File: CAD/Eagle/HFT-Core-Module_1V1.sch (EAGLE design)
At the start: 399 parts, among them Q0521 ABS07-32.768KHZ, Q0811 ABM03B-32.000MHZ, Q0911 ABM3B-16MHZ-10-R50-1-U, T1201 MMBT2222, T1202 MMBT2222, T1203 MMBT2222, U0111 STM32L4Z_144PIN_SMPS, U0431 PAM2305AAB120, U0601 LM4120IM5-3.0, U0611 MAX5217, U0631 CFPT-141-20MHZ, U0641 OPA354, U0701 Si5338, U0801 SX1276, U0901 AX5243, U0911 PE4259, U0921 PE4259, U0991 PE4259, U1101 MCP3911A0-E-SS, U1111 MAX5136AGTG+, U1121 OPA354, U1131 OPA354, U1141 OPA354, U1201 NHD-C0220BIZ_2X20CHARS, U1301 MPU-9250, U1311 MS5607-02BA03, U1321 SHT31-DIS, U1402 SPV1040T, U1501 TS5A23166, U1601 SC189ZSKTRT, U1701 TS5A23166, U1801 TS5A23166, U1901 TS5A23166, X1261 TTE_EN11-HSM, X1401 WIRE-TO-BOARD_5MM08_1X02, X2001 MOLEX 105017-0001, X2101 SMA_SMT_AMPHENOL-901-143, SAM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, X2111 SMA_SMT_AMPHENOL-901-143, SAM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, X2201 CUI SJ1-3535NS, X2211 CUI SJ1-3535NS, X2311 2X20/90_1MM27_HARWIN_M50-3202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, X2312 2X20/90_1MM27_HARWIN_M50-3202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, X2321 2X20/90_1MM27_HARWIN_M50-3202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, X2322 2X20/90_1MM27_HARWIN_M50-3202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, X2331 2X20/90_1MM27_HARWIN_M50-3202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, X2332 2X20/90_1MM27_HARWIN_M50-3202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

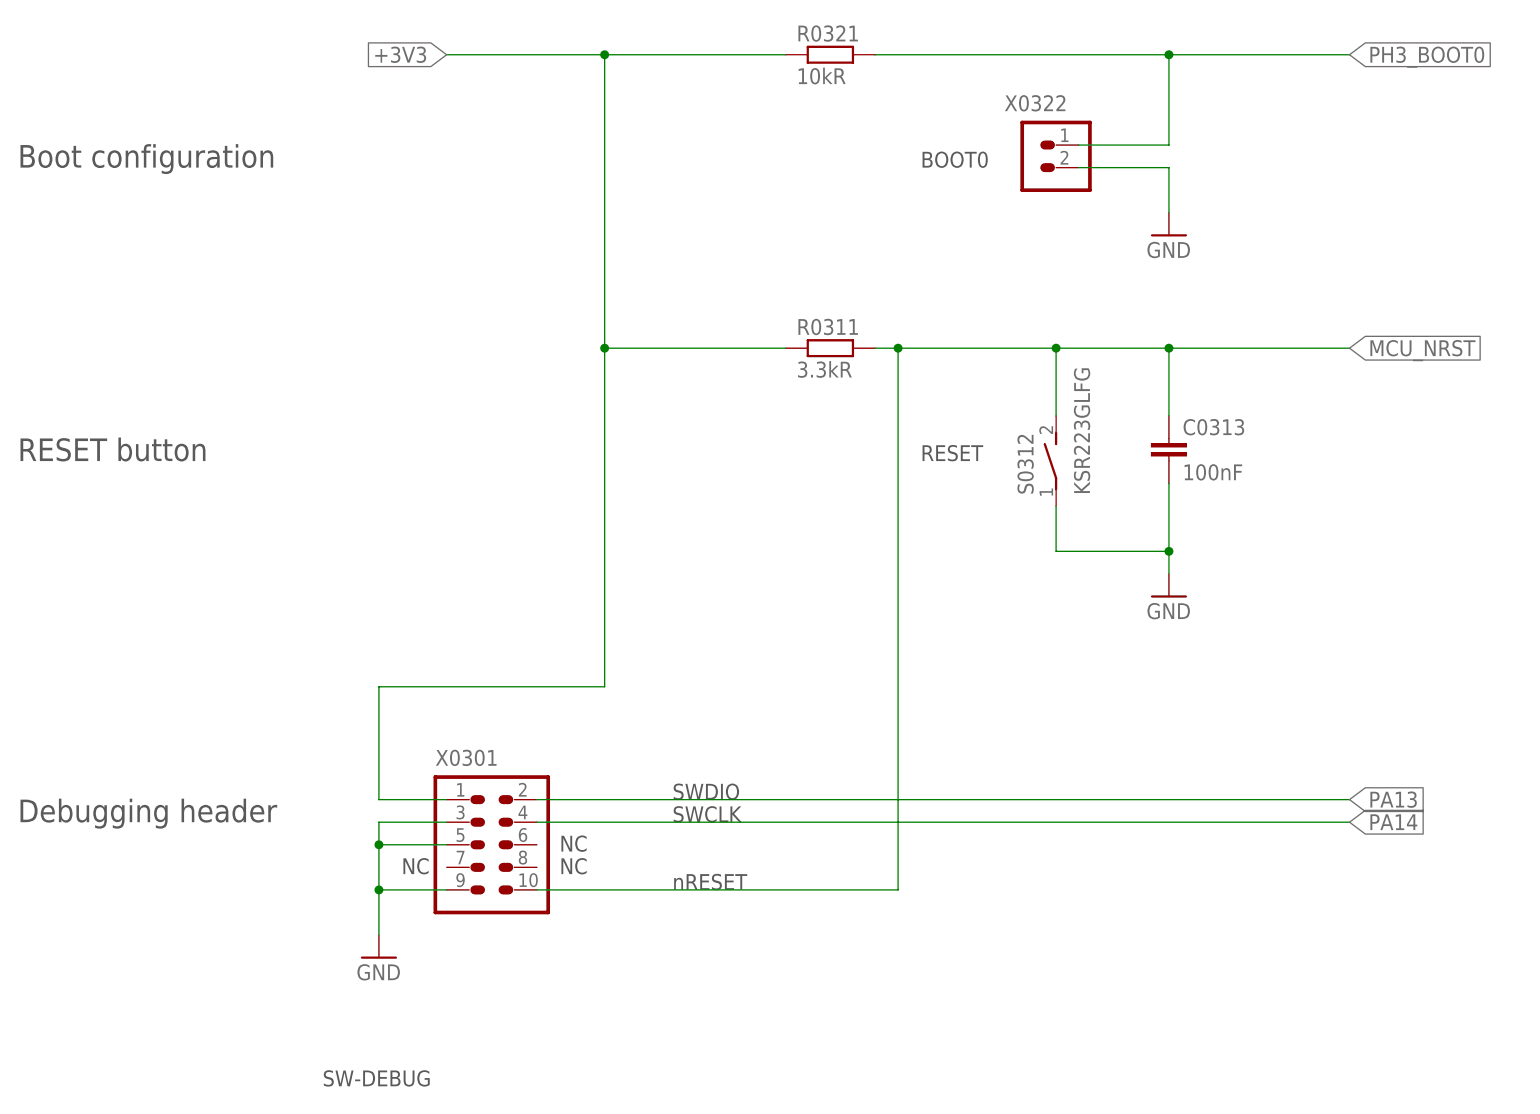
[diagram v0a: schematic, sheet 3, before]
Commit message: HW_1V1 - SWD header, XO 32.768kHz caps, RESET resistor removed, SWD resistors added
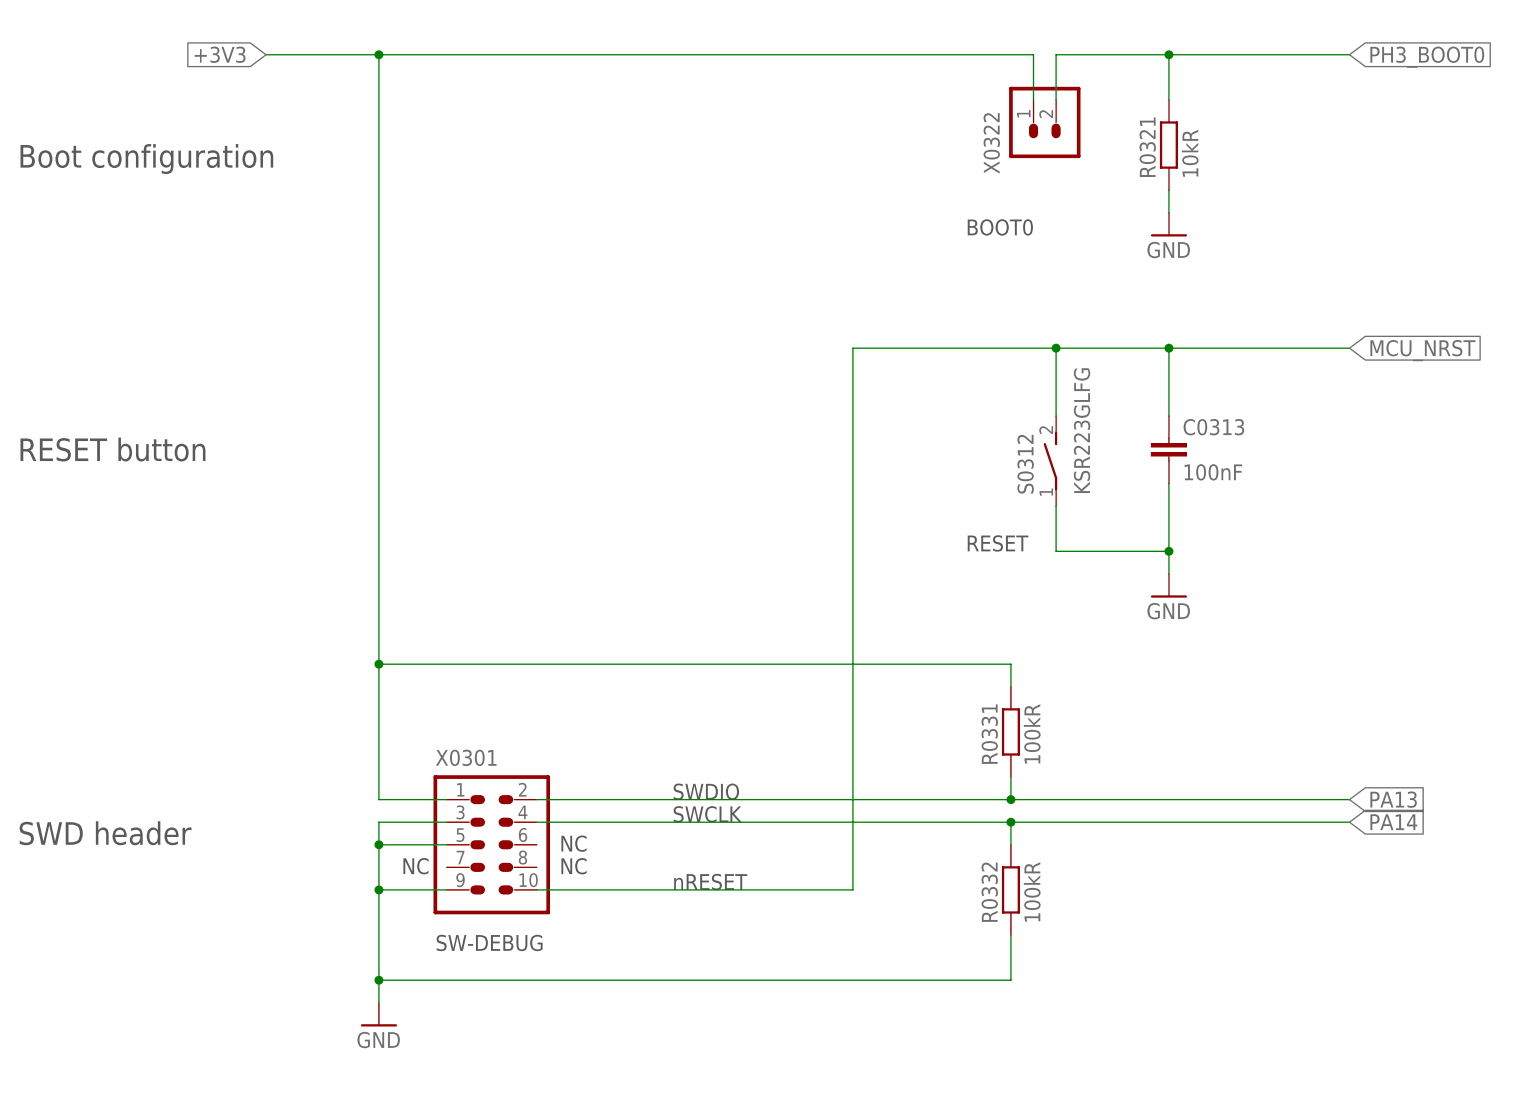
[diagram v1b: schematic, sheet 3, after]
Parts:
- removed R0311: 3.3kR, rcl:R-EU_R0603
- added C0532: 12pF, rcl:C-EUC0603
- added R0331, R0332: 100kR, rcl:R-EU_R0603
- C0511: value 1.5pF -> 18pF
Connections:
- net +3V3: now also R0331.2, X0322.1; no longer R0311.1, R0321.1
- net GND: now also C0532.2, R0321.1, R0332.1; no longer X0322.2
- net MCU_NRST: no longer R0311.2
- net PA13: now also R0331.1
- net PA14: now also R0332.2
- net PC14_MCU_OSC32_IN: now also C0532.1
- net PH3_BOOT0: now also X0322.2; no longer X0322.1
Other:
- note added: "SWD header"
- note removed: "Debugging header"
- moved on the sheet: R0321, X0322

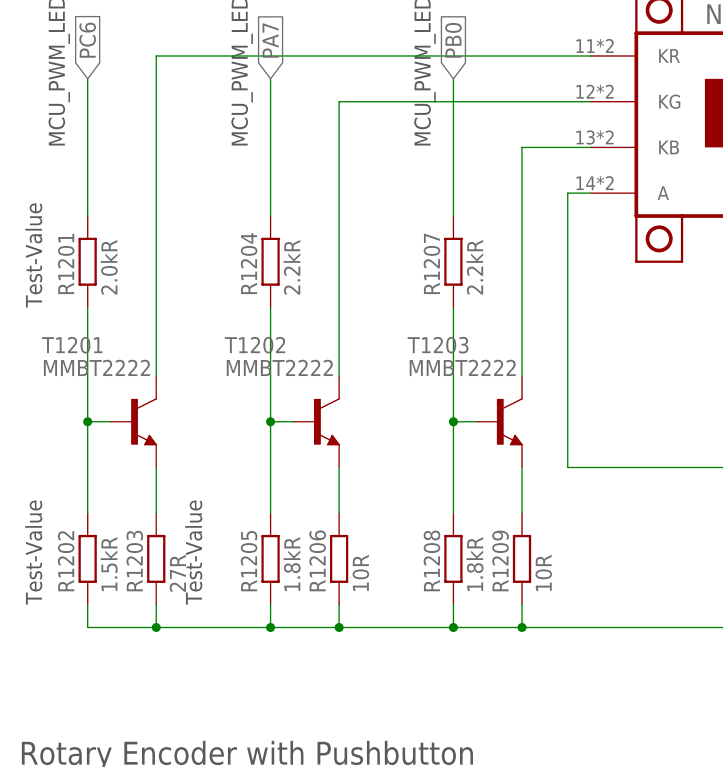
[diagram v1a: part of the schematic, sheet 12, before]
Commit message: HW_1V1 - LCD-backlight resistors changed
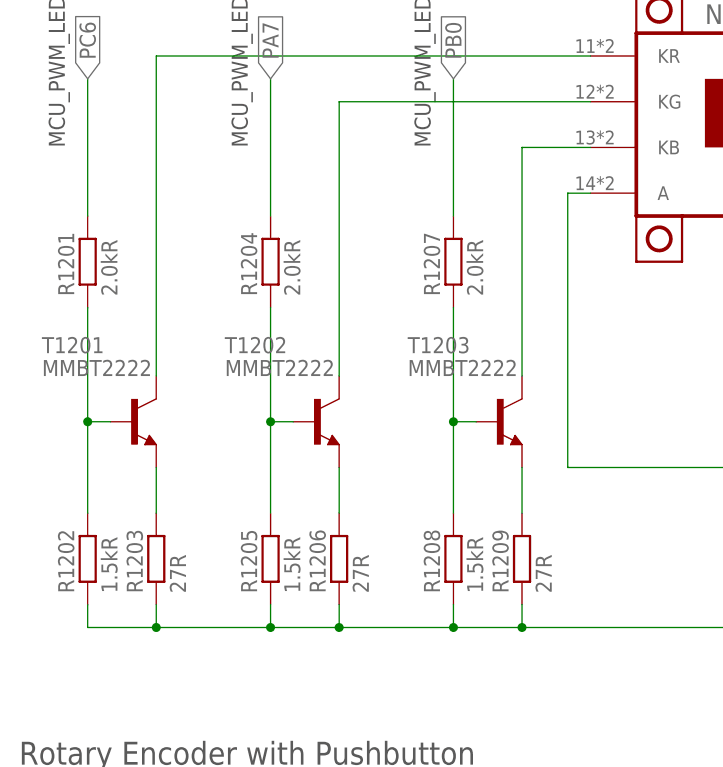
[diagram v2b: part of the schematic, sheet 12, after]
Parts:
- R1204, R1207: value 2.2kR -> 2.0kR
- R1205, R1208: value 1.8kR -> 1.5kR
- R1206, R1209: value 10R -> 27R
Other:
- note removed: "Test-Value"
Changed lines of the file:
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@@
 <part name="T1202" library="transistor" deviceset="BC846" device="" value="MMBT2222"/>
 <part name="T1203" library="transistor" deviceset="BC846" device="" value="MMBT2222"/>
-<part name="R1209" library="rcl" deviceset="R-EU_" device="R0805" value="10R"/>
-<part name="R1208" library="rcl" deviceset="R-EU_" device="R0603" value="1.8kR"/>
-<part name="R1207" library="rcl" deviceset="R-EU_" device="R0603" value="2.2kR"/>
-<part name="R1206" library="rcl" deviceset="R-EU_" device="R0805" value="10R"/>
+<part name="R1209" library="rcl" deviceset="R-EU_" device="R0805" value="27R"/>
+<part name="R1208" library="rcl" deviceset="R-EU_" device="R0603" value="1.5kR"/>
+<part name="R1207" library="rcl" deviceset="R-EU_" device="R0603" value="2.0kR"/>
+<part name="R1206" library="rcl" deviceset="R-EU_" device="R0805" value="27R"/>
 <part name="R1203" library="rcl" deviceset="R-EU_" device="R0805" value="27R"/>
-<part name="R1205" library="rcl" deviceset="R-EU_" device="R0603" value="1.8kR"/>
+<part name="R1205" library="rcl" deviceset="R-EU_" device="R0603" value="1.5kR"/>
 <part name="R1202" library="rcl" deviceset="R-EU_" device="R0603" value="1.5kR"/>
-<part name="R1204" library="rcl" deviceset="R-EU_" device="R0603" value="2.2kR"/>
+<part name="R1204" library="rcl" deviceset="R-EU_" device="R0603" value="2.0kR"/>
 <part name="R1201" library="rcl" deviceset="R-EU_" device="R0603" value="2.0kR"/>
 <part name="FRAME_13" library="df4iah_frame" deviceset="A4L-LOC" device="" value="Holes"/>
@@
 <text x="195.58" y="53.34" size="1.778" layer="97">MCU_IN_RE_Q</text>
 <text x="195.58" y="35.56" size="1.778" layer="97">MCU_IN_RE_PB</text>
-<text x="12.7" y="88.9" size="1.778" layer="97" rot="R90">Test-Value</text>
-<text x="12.7" y="121.92" size="1.778" layer="97" rot="R90">Test-Value</text>
-<text x="30.48" y="88.9" size="1.778" layer="97" rot="R90">Test-Value</text>
 </plain>
 <instances>

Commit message: HW_1V1 - I2C addresses changed, LCD will be replaced by EA DOGS104N-A
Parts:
- R1331, R1332: value 3.9kR -> 1.0kR
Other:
- note added: "9-axis sensor: MPU-9250 I2C addr: 0x68 / 0x0C"
- note added: "Baro sensor: MS5607-02BA03 I2C addr: 0x76"
- note added: "Clock distributor I2C addr: 0x70"
- note added: "LC-Display I2C addr: 0x3D"
- note added: "LCD: 2x20 chars NHD-C0220BIZ-FS(RGB)-FBW-3VM-ND to be replaced by: LCD: 4x10 chars EA DOGS104N-A (Mouser: 790-EADOGS104N-A)"
- note added: "RH sensor: Sensirion SHT3x I2C addr: 0x44"
- note removed: "9-axis sensor: MPU-9250"
- note removed: "Baro sensor: MS5607-02BA03"
- note removed: "Clock distributor I2C addr: 0xE0/0xE1"
- note removed: "I2C address = 1000100"
- note removed: "I2C address = 1101000"
- note removed: "I2C address = 1110110"
- note removed: "LC-Display I2C addr: 0x7C/0x7D"
- note removed: "LCD: 2x20 chars NHD-C0220BIZ-FS(RGB)-FBW-3VM-ND"
- note removed: "RH sensor: Sensirion SHT3x"
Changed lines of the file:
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@@
 <part name="R1301" library="rcl" deviceset="R-EU_" device="R0603" value="68R"/>
 <part name="C1302" library="rcl" deviceset="C-EU" device="C0603" value="10nF"/>
-<part name="R1331" library="rcl" deviceset="R-EU_" device="R0603" value="3.9kR"/>
-<part name="R1332" library="rcl" deviceset="R-EU_" device="R0603" value="3.9kR"/>
+<part name="R1331" library="rcl" deviceset="R-EU_" device="R0603" value="1.0kR"/>
+<part name="R1332" library="rcl" deviceset="R-EU_" device="R0603" value="1.0kR"/>
 <part name="GND1311" library="df4iah_supply" deviceset="GND" device=""/>
 <part name="C1311" library="rcl" deviceset="C-EU" device="C0603" value="100nF"/>
@@
 <text x="116.84" y="137.16" size="1.778" layer="97" rot="R90">Impedance 100 Ohms</text>
 <text x="22.86" y="162.56" size="2.54" layer="97" ratio="15">Clock distributor
-I2C addr: 0xE0/0xE1</text>
+I2C addr: 0x70</text>
 <text x="118.364" y="38.1" size="1.778" layer="97" rot="R90">10MHz</text>
 <text x="50.8" y="88.9" size="1.778" layer="97">16MHz</text>
@@
 <description>LCD / Encoder</description>
 <plain>
-<text x="160.02" y="139.7" size="1.778" layer="97">LCD: 2x20 chars  NHD-C0220BIZ-FS(RGB)-FBW-3VM-ND</text>
+<text x="160.02" y="139.7" size="1.778" layer="97">LCD: 2x20 chars  NHD-C0220BIZ-FS(RGB)-FBW-3VM-ND
+to be replaced by:
+LCD: 4x10 chars EA DOGS104N-A (Mouser: 790-EADOGS104N-A)</text>
 <text x="22.86" y="162.56" size="2.54" layer="97" ratio="15">LC-Display
-I2C addr: 0x7C/0x7D</text>
+I2C addr: 0x3D</text>
 <text x="10.16" y="71.12" size="2.54" layer="97" ratio="15">Rotary Encoder with Pushbutton</text>
 <text x="15.24" y="139.7" size="1.778" layer="97" rot="R90">MCU_PWM_LED_R</text>
@@
 <description>I2C Sensors</description>
 <plain>
-<text x="22.86" y="162.56" size="2.54" layer="97" ratio="15">Baro sensor: MS5607-02BA03</text>
-<text x="22.86" y="81.28" size="2.54" layer="97" ratio="15">9-axis sensor: MPU-9250</text>
+<text x="22.86" y="162.56" size="2.54" layer="97" ratio="15">Baro sensor: MS5607-02BA03
+I2C addr: 0x76</text>
+<text x="22.86" y="81.28" size="2.54" layer="97" ratio="15">9-axis sensor: MPU-9250
+I2C addr: 0x68 / 0x0C</text>
 <text x="116.84" y="66.04" size="1.778" layer="97">NC</text>
 <text x="116.84" y="63.5" size="1.778" layer="97">NC</text>
-<text x="83.82" y="38.1" size="1.778" layer="97">I2C address = 1101000</text>
-<text x="47.752" y="104.902" size="1.778" layer="97">I2C address = 1110110</text>
 <text x="85.598" y="118.364" size="1.778" layer="97">NC</text>
 <text x="85.598" y="123.444" size="1.778" layer="97">NC</text>
-<text x="149.86" y="162.56" size="2.54" layer="97" ratio="15">RH sensor: Sensirion SHT3x</text>
-<text x="160.02" y="93.98" size="1.778" layer="97">I2C address = 1000100</text>
+<text x="149.86" y="162.56" size="2.54" layer="97" ratio="15">RH sensor: Sensirion SHT3x
+I2C addr: 0x44</text>
 <text x="195.58" y="81.28" size="2.54" layer="97" ratio="15">I2C4 Termination</text>
 <text x="127" y="25.4" size="1.778" layer="97">I2C2_INT</text>
